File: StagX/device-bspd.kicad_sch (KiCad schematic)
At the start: 1 part

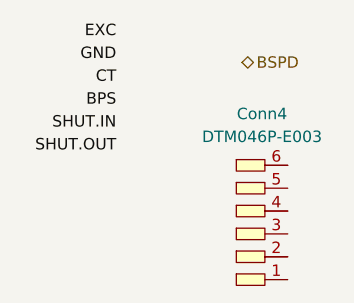
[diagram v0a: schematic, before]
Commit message: Completed shutdown loop
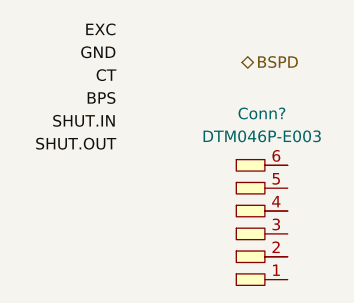
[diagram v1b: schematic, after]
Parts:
- renumbered Conn4 to Conn?
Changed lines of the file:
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@@
   (symbol (lib_id "Connectors_SUFST:Deutsch_DTM_6P_Pin") (at 141.605 95.885 0) (unit 1)
     (in_bom yes) (on_board yes) (dnp no) (fields_autoplaced)
-    (property "Reference" "Conn4" (at 140.6525 94.615 0)
+    (property "Reference" "Conn?" (at 140.6525 94.615 0)
       (effects (font (size 1.27 1.27)))
     )
@@
       (project "StagX"
         (path "/03011643-0690-4b85-ab78-d6a62dae52b1/ac5342b2-3f31-4ced-840e-357d9fbb572e"
-          (reference "Conn4") (unit 1)
+          (reference "Conn?") (unit 1)
         )
       )
